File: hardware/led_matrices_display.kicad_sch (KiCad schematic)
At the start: 4 parts, among them U11 KWM-20882CUYB, U12 KWM-20882CUYB, U13 KWM-20882CUYB, U14 KWM-20882CUYB

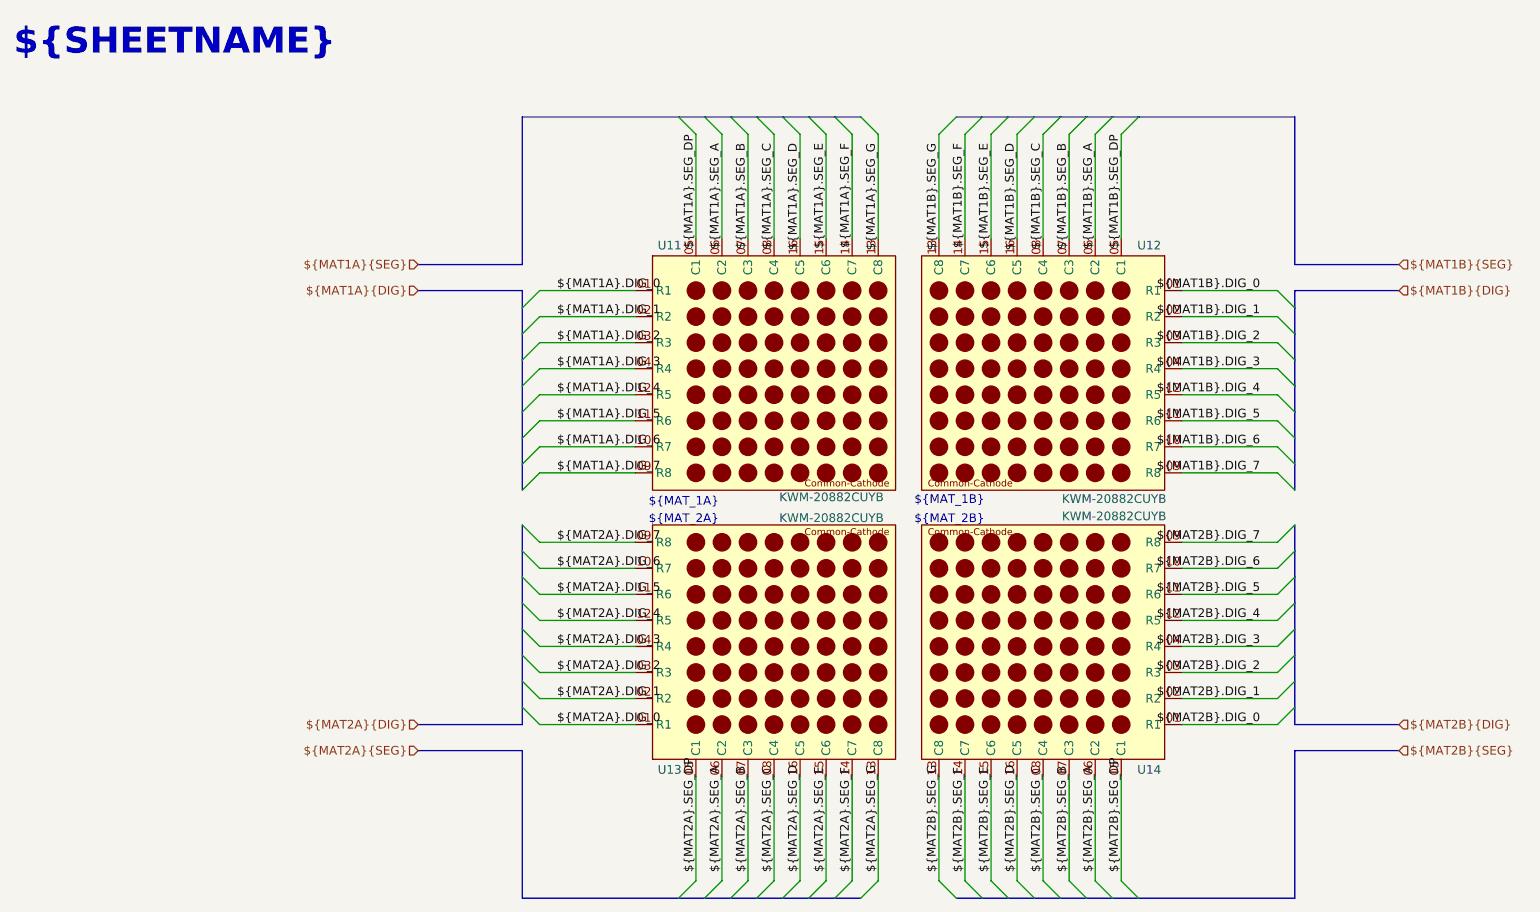
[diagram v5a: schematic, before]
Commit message: Reviewed the Fields Table and marked all components that should not be populated. Then I runned rules check in the schematic and PCB
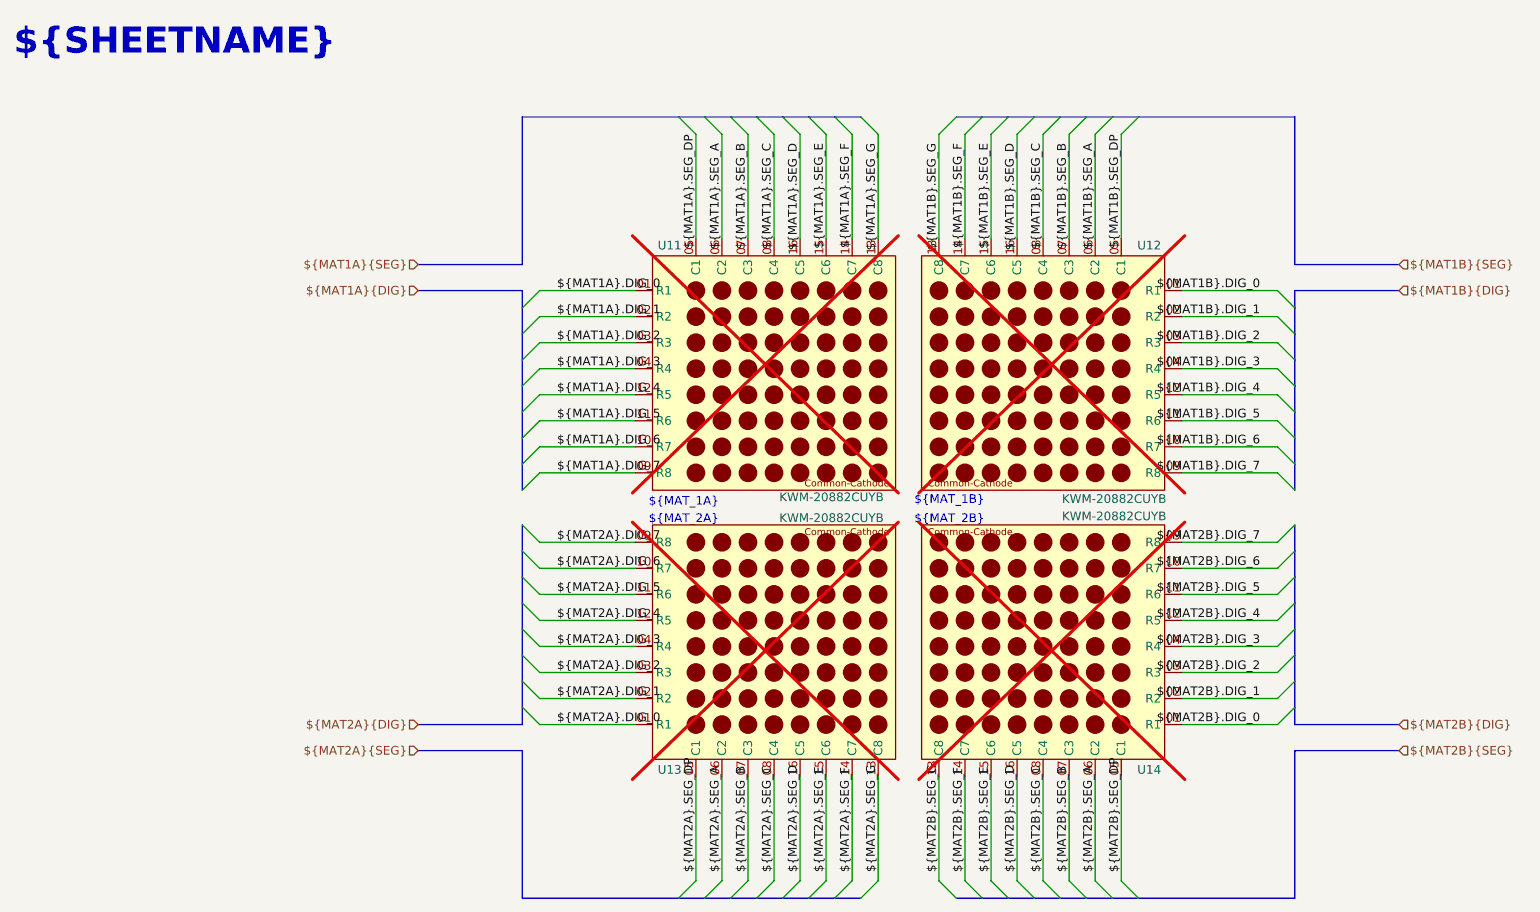
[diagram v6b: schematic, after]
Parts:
- U11, U12, U13, U14: now not fitted
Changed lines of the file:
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@@
 		(in_bom no)
 		(on_board yes)
-		(dnp no)
+		(dnp yes)
 		(property "Reference" "U14"
 			(at 186.182 128.524 0)
@@
 		(in_bom no)
 		(on_board yes)
-		(dnp no)
+		(dnp yes)
 		(property "Reference" "U12"
 			(at 186.182 51.816 0)
@@
 		(in_bom no)
 		(on_board yes)
-		(dnp no)
+		(dnp yes)
 		(property "Reference" "U13"
 			(at 112.522 128.524 0)
@@
 		(in_bom no)
 		(on_board yes)
-		(dnp no)
+		(dnp yes)
 		(property "Reference" "U11"
 			(at 112.522 51.816 0)
